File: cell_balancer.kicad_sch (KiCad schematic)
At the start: 40 parts, among them Q1 AO3400A, Q2 AO3400A, U4 CSD25402Q3A, U5 BQ7791500PWR

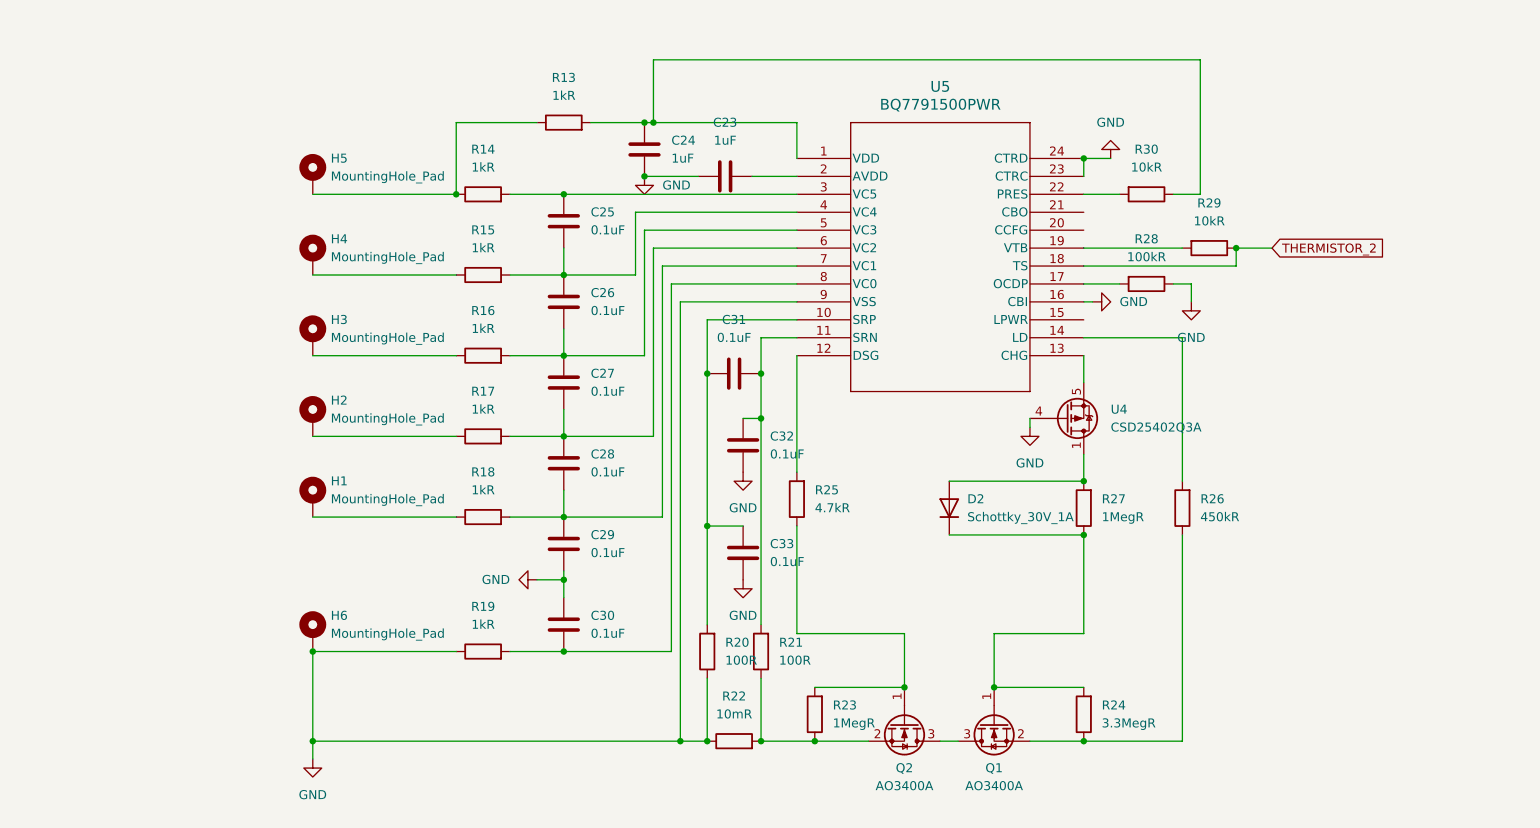
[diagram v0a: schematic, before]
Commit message: Finish schematic
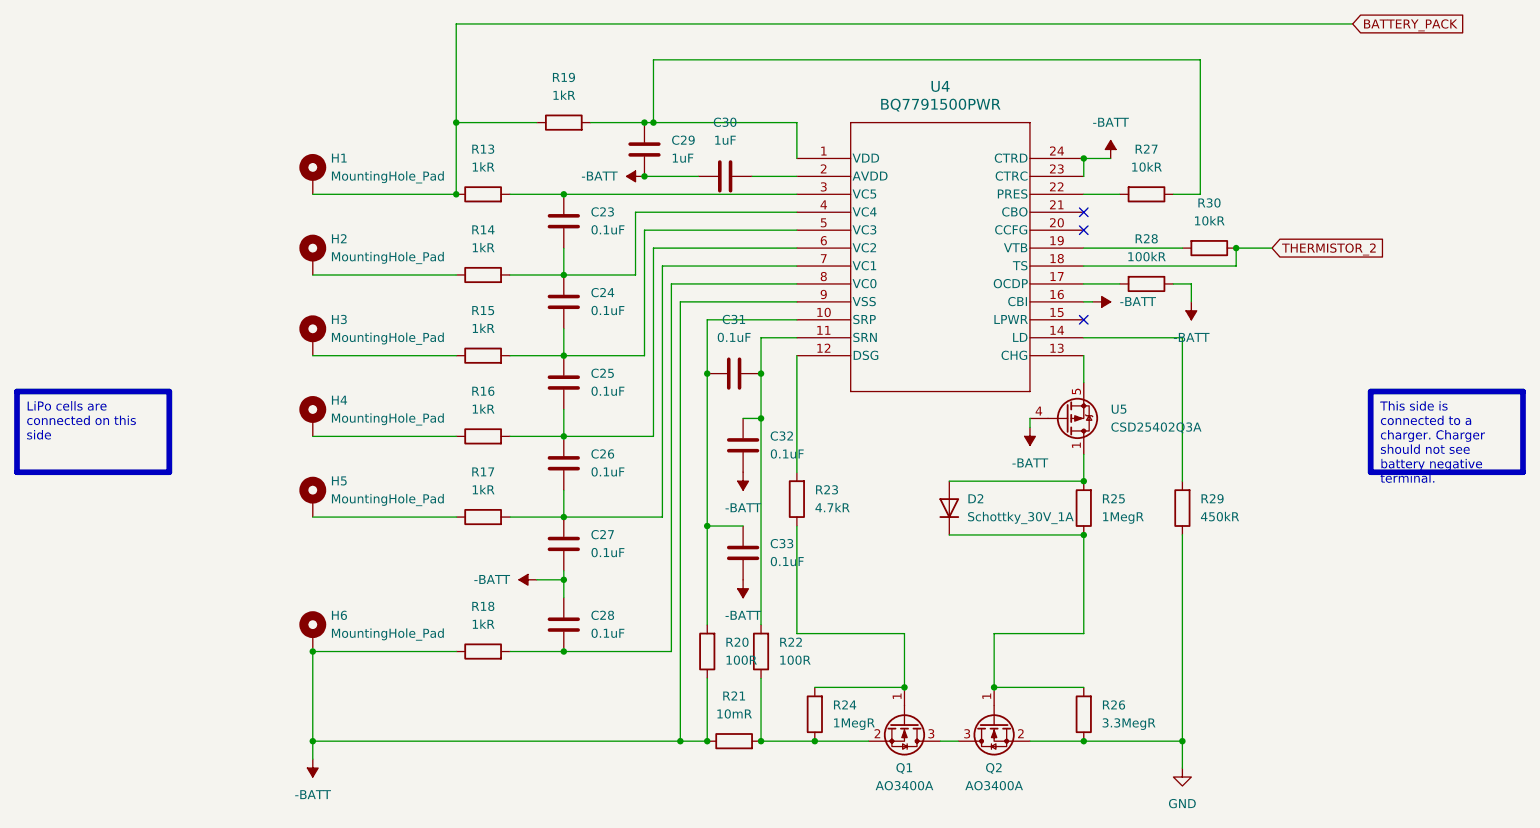
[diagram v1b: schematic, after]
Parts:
- renumbered C25 to C23, C26 to C24, C27 to C25, C28 to C26, C29 to C27, C30 to C28, C24 to C29, C23 to C30, H5 to H1, H4 to H2, H2 to H4, H1 to H5, Q2 to Q1, Q1 to Q2, R14 to R13, R15 to R14, R16 to R15, R17 to R16, R18 to R17, R19 to R18, R13 to R19, R22 to R21, R21 to R22, R25 to R23, R23 to R24, R27 to R25, R24 to R26, R30 to R27, R26 to R29, R29 to R30, U5 to U4, U4 to U5
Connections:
- net GND: now also Q2.2 (S), R26.1, R29.1; no longer C27.1, C28.2, C29.1, C30.1, C32.2, C33.2, H6.1, R18.1, R20.1, R21.1, R28.1, U4.16 (CBI), U4.23 (CTRC), U4.24 (CTRD), U4.9 (VSS), U5.4 (G)
- net BATTERY_PACK: now reaches H1.1, R13.1, R19.1
- new net -BATT: C27.1, C28.2, C29.1, C30.1, C32.2, C33.2, H6.1, R18.1, R20.1, R21.1, R28.1, U4.16 (CBI), U4.23 (CTRC), U4.24 (CTRD), U4.9 (VSS), U5.4 (G)
- no-connect marks 0 -> 3

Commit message: First layout
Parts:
- H1, H2, H3, H4, H6: footprint (none) -> TestPoint:TestPoint_THTPad_2.5x2.5mm_Drill1.2mm
- H5: footprint MountingHole:MountingHole_2.2mm_M2_DIN965_Pad_TopBottom -> TestPoint:TestPoint_THTPad_2.5x2.5mm_Drill1.2mm
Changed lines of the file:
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@@
 			)
 		)
-		(property "Footprint" ""
+		(property "Footprint" "TestPoint:TestPoint_THTPad_2.5x2.5mm_Drill1.2mm"
 			(at 66.04 57.15 0)
 			(effects
@@
 			)
 		)
-		(property "Footprint" ""
+		(property "Footprint" "TestPoint:TestPoint_THTPad_2.5x2.5mm_Drill1.2mm"
 			(at 66.04 110.49 0)
 			(effects
@@
 			)
 		)
-		(property "Footprint" ""
+		(property "Footprint" "TestPoint:TestPoint_THTPad_2.5x2.5mm_Drill1.2mm"
 			(at 66.04 80.01 0)
 			(effects
@@
 			)
 		)
-		(property "Footprint" ""
+		(property "Footprint" "TestPoint:TestPoint_THTPad_2.5x2.5mm_Drill1.2mm"
 			(at 66.04 68.58 0)
 			(effects
@@
 			)
 		)
-		(property "Footprint" ""
+		(property "Footprint" "TestPoint:TestPoint_THTPad_2.5x2.5mm_Drill1.2mm"
 			(at 66.04 45.72 0)
 			(effects
@@
 			)
 		)
-		(property "Footprint" "MountingHole:MountingHole_2.2mm_M2_DIN965_Pad_TopBottom"
+		(property "Footprint" "TestPoint:TestPoint_THTPad_2.5x2.5mm_Drill1.2mm"
 			(at 66.04 91.44 0)
 			(effects
